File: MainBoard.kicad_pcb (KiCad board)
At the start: 2 copper layers, 120 x 68 mm, 79 parts, among them J1 DB25, P1 BOOT, P10 CONN_01X03, P11 CONN_01X03, P12 CONN_01X03, P13 CONN_01X03, P14 CONN_01X02, P15 CONN_02X07, P16 CONN_02X04, P18 CONN_01X03, P2 CONN_01X04, P3 CONN_02X04, P4 HOLE, P5 HOLE, P6 HOLE, P7 HOLE, P8 CONN_01X02, P9 CONN_01X03, Q1 BSS138, Q2 BSS138, Q3 DMN65D8L, SW1 RESET, U1 mp2307, U10 SI4425DDY, U2 DYS_mini_ESC, U3 DYS_mini_ESC, U4 DYS_mini_ESC, U5 DYS_mini_ESC, U6 TLV1117LV33, U7 TENDA_P200, U8 pca9685, U9 STM32F103CBT6, Y1 8MHz

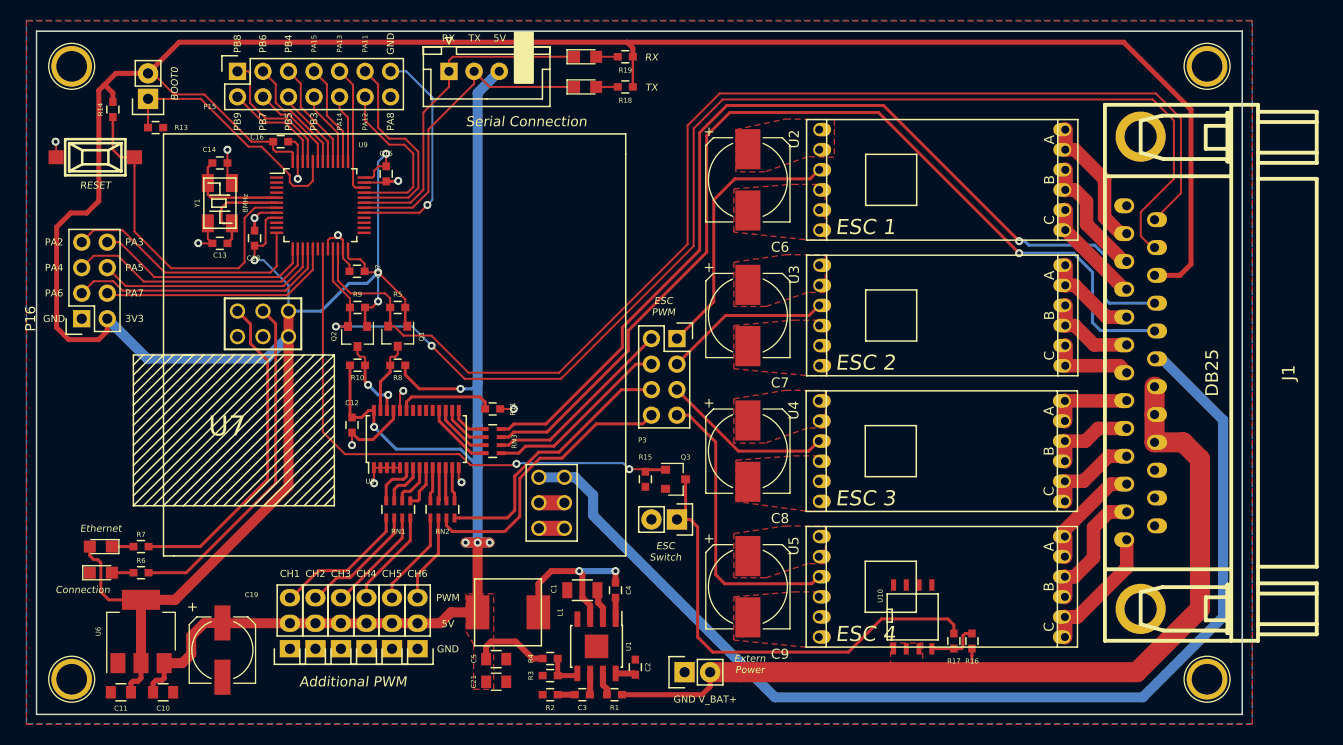
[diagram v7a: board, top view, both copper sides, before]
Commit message: Add current & voltage sensor
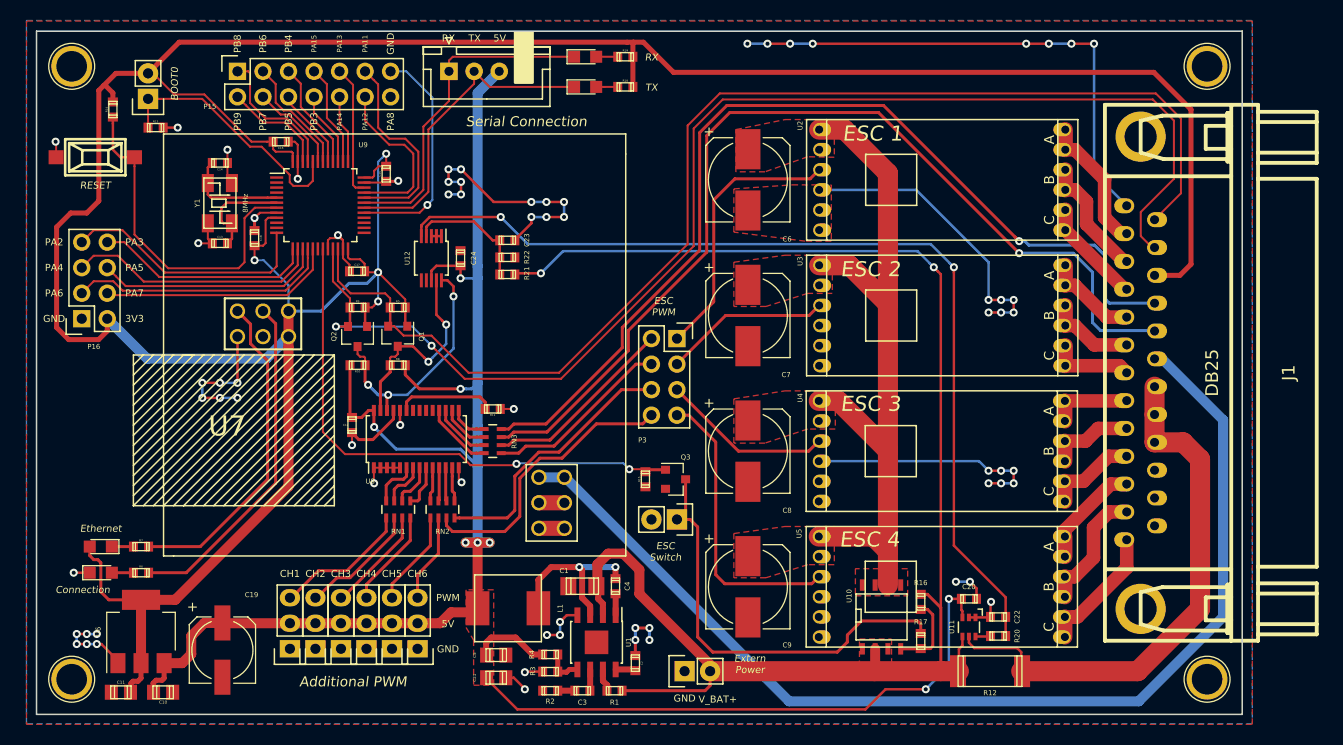
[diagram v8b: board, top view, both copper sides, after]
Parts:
- added C20: 0.1uF, footprint:c_0603, F.Cu at (172.8, 106.5)
- added C22: 1uF, footprint:c_0603, F.Cu at (175.7, 108.3)
- added C23: 0.1uF, footprint:c_0603, F.Cu at (126.9, 70.8)
- added C24: 0.1uF, footprint:c_0603, F.Cu at (122.2, 72.6)
- added R12: 0.003 %1, footprint:r_2512, F.Cu at (174.9, 113.7)
- added R20: 3.3k, footprint:r_0603, F.Cu at (175.7, 110.2)
- added R21: 30.1k %1, footprint:r_0603, F.Cu at (126.9, 74.2)
- added R22: 10k %1, footprint:r_0603, F.Cu at (126.9, 72.5)
- added U11: INA199A2, TO_SOT_Packages_SMD:SC-70-6, F.Cu at (172.8, 109.3)
- added U12: ADS1015, Housings_SSOP:MSOP-10_3x3mm_Pitch0.5mm, F.Cu at (119.3, 72.6)
- C1: footprint Capacitors_SMD:C_1206 -> footprint:c_1206
- C10, C11, C21, C5: footprint Capacitors_SMD:C_0805 -> footprint:c_0805
- C12, C15, C16, C17, C18, C2, C3, C4: footprint Capacitors_SMD:C_0603 -> footprint:c_0603
- C13, C14: value 33uF -> 33pF; footprint Capacitors_SMD:C_0603 -> footprint:c_0603
- R1, R10, R11, R13, R14, R15, R16, R17, R18, R19, R2, R3, R4, R5, R6, R7, R8, R9: footprint Capacitors_SMD:C_0603 -> footprint:r_0603
- moved R16 6.42 mm to (168.0, 106.8)
- moved R17 3.30 mm to (168.0, 110.7), turned to 270 degrees
- moved U10 3.10 mm to (164.1, 108.3)
- moved C1 0.40 mm to (134.3, 105.2), turned to 0 degrees
- moved C21 0.40 mm to (125.8, 114.3), turned to 180 degrees
- moved C4 0.40 mm to (137.6, 105.2), turned to 90 degrees
- moved C5 0.40 mm to (125.8, 112.1), turned to 180 degrees
- moved R3 0.40 mm to (131.1, 113.7), turned to 0 degrees
- moved R4 0.40 mm to (131.1, 112.0), turned to 180 degrees
- moved C2 0.40 mm to (139.6, 112.9), turned to 270 degrees
- moved C3 0.40 mm to (134.3, 115.6), turned to 0 degrees
- moved L1 0.40 mm to (126.9, 107.4)
- moved R1 0.40 mm to (137.5, 115.6), turned to 0 degrees
- moved R2 0.40 mm to (131.1, 115.6), turned to 0 degrees
- moved U1 0.40 mm to (135.7, 110.8)
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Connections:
- J1 pad 17: /V_BAT -> /V_IN
- J1 pad 18: /V_BAT -> /V_IN
- J1 pad 19: /V_BAT -> /V_IN
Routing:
- net GND: track 50.6 -> 227.5 mm, vias 12 -> 70
- net /ADC_I: track 0.00 -> 95.3 mm, vias 0 -> 2
- net /V_PWR: track 1.50 -> 76.0 mm
- net /5V: track 135.7 -> 201.3 mm, vias 5 -> 8
- net /V_BAT: track 93.0 -> 151.0 mm, vias 0 -> 2
- net /V_IN: track 0.00 -> 54.1 mm
- net /SCL_5V: track 8.55 -> 24.6 mm, vias 2 -> 3
- net /SDA_5V: track 7.54 -> 20.5 mm, vias 0 -> 2
- net /ADC_V: track 0.00 -> 12.6 mm
- net Net-(P14-Pad1): track 46.3 -> 43.3 mm
- net Net-(R16-Pad2): track 5.29 -> 7.85 mm
- net Net-(R20-Pad2): track 0.00 -> 1.52 mm
- net /T+: track 110.6 -> 109.8 mm
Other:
- net class Default: clearance 0.2 -> 0.15; trace_width 0.3 -> 0.25
- rule trace_clearance: 0.2 -> 0.15
